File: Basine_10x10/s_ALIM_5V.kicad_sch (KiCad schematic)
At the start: 25 parts, among them U17 TPS5430DDA

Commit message: Basine_10x10
ajout symbole ultrogothe
ajout power flag sur 5V
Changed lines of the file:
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@@
 	(wire
 		(pts
-			(xy 102.87 127) (xy 105.41 127)
+			(xy 102.87 127) (xy 116.84 127)
 		)
 		(stroke
@@
 					(unit 1)
 				)
+			)
+		)
+	)
+	(symbol
+		(lib_name "PWR_FLAG_1")
+		(lib_id "power:PWR_FLAG")
+		(at 116.84 127 0)
+		(unit 1)
+		(exclude_from_sim no)
+		(in_bom yes)
+		(on_board yes)
+		(dnp no)
+		(fields_autoplaced yes)
+		(property "Reference" "#FLG01"
+			(at 116.84 125.095 0)
+			(effects
+				(font
+					(size 1.27 1.27)
+				)
+				(hide yes)
+			)
+		)
+		(property "Value" "PWR_FLAG"
+			(at 116.84 121.92 0)
+			(effects
+				(font
+					(size 1.27 1.27)
+				)
+			)
+		)
+		(property "Footprint" ""
+			(at 116.84 127 0)
+			(effects
+				(font
+					(size 1.27 1.27)
+				)
+				(hide yes)
+			)
+		)
+		(property "Datasheet" "~"
+			(at 116.84 127 0)
+			(effects
+				(font
+					(size 1.27 1.27)
+				)
+				(hide yes)
+			)
+		)
+		(property "Description" "Special symbol for telling ERC where power comes from"
+			(at 116.84 127 0)
+			(effects
+				(font
+					(size 1.27 1.27)
+				)
+				(hide yes)
+			)
+		)
+		(pin "1"
+		)
+		(instances
+			(project "Basine"
+				(path "/e63e39d7-6ac0-4ffd-8aa3-1841a4541b55/c0a1413d-0c72-4618-8b9b-4221cc6761bc"
+					(reference "#FLG01")
+					(unit 1)
+				)

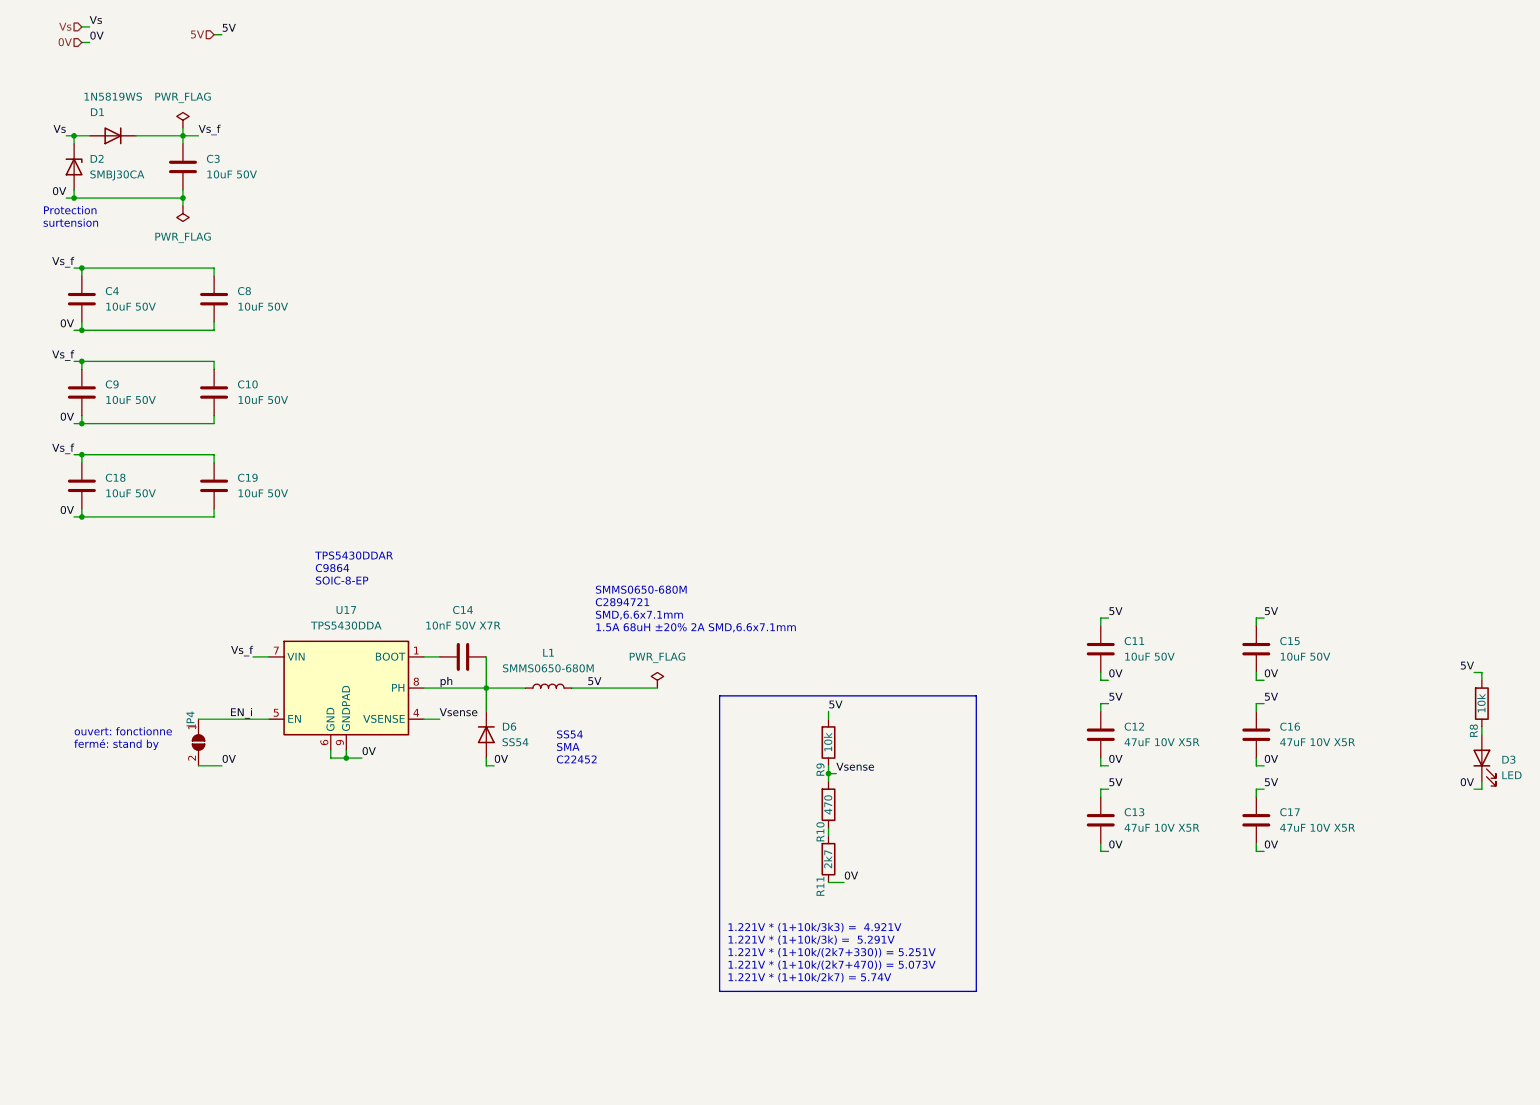
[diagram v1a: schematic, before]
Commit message: 10x10
alim 5V ok
placement et routage ok
reste vias à placer
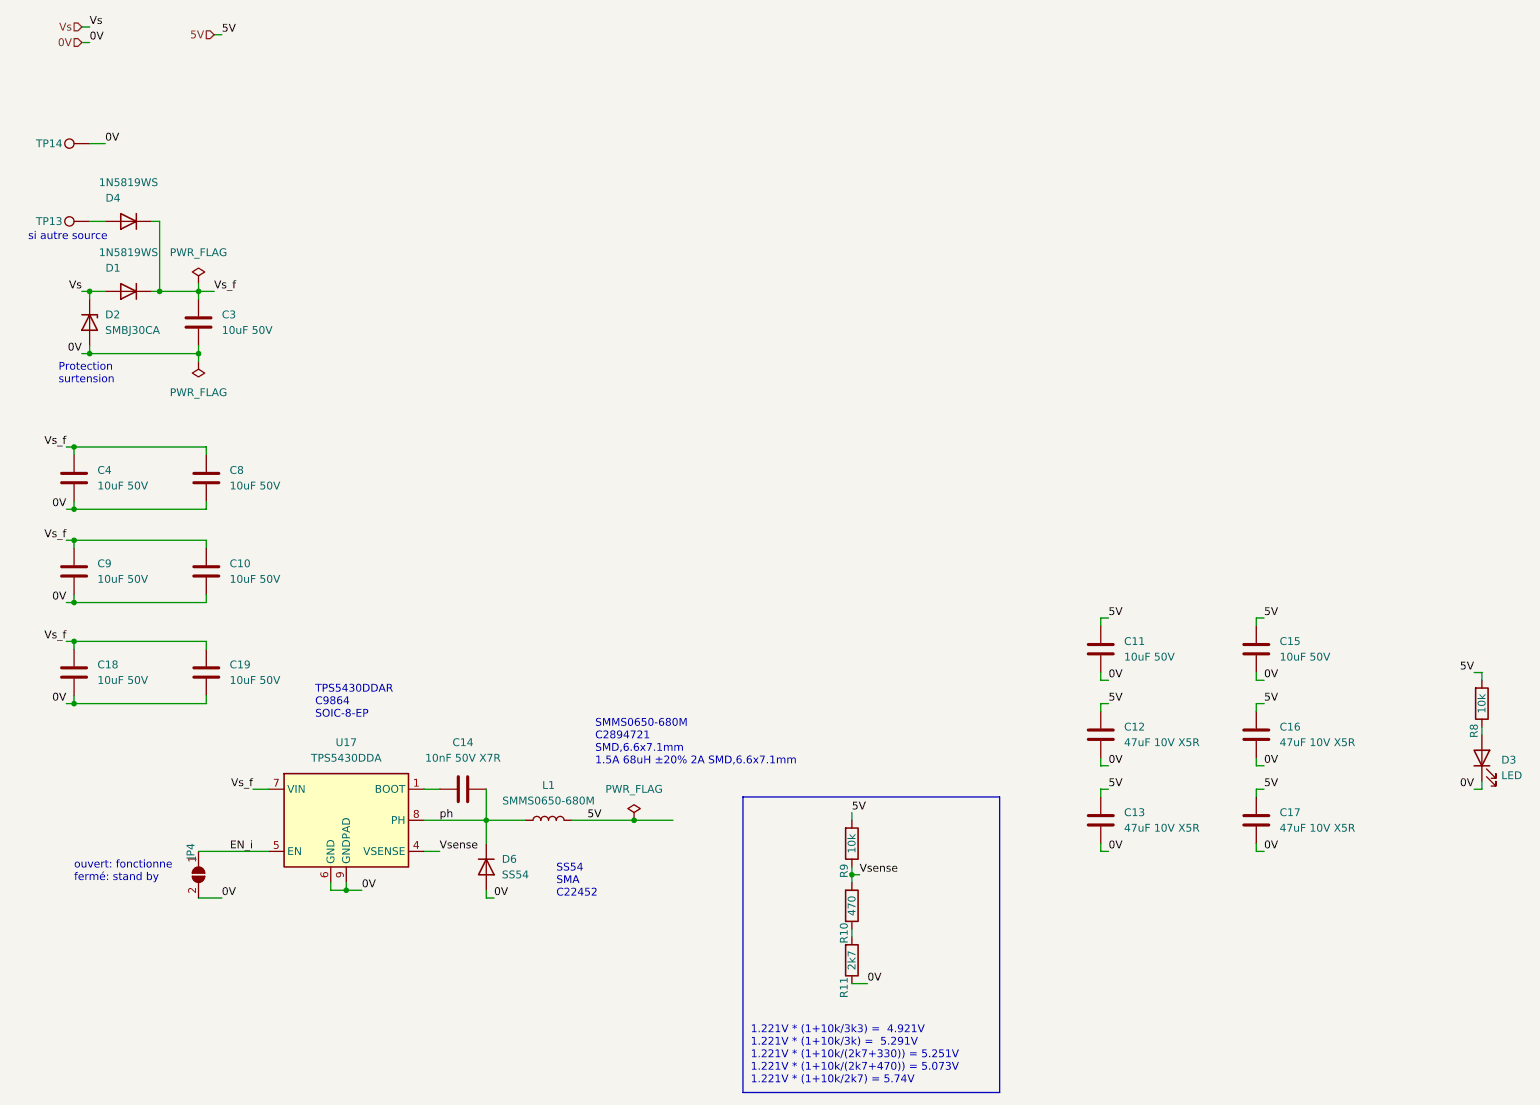
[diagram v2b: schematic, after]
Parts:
- added D4: 1N5819WS, Diode_SMD:D_SOD-323, symbol Device:D
- added TP13, TP14: TestPoint, Chimere_comps:Pastille, symbol Connector:TestPoint
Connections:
- net 0V: now also TP14.1
- net Vs_f: now also D4.1 (K)
- new net: D4.2 (A), TP13.1
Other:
- note added: "si autre source"
- moved on the sheet: C10, C14, C18, C19, C3, C4, C8, C9, D1, D2, D6, JP4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

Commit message: 10x10
tentative de fabrication
pénurie spring clamp à gérer
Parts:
- JP4, TP13, TP14: now left out of the parts list
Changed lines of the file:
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@@
 		(unit 1)
 		(exclude_from_sim no)
-		(in_bom yes)
+		(in_bom no)
 		(on_board yes)
 		(dnp no)
@@
 		(unit 1)
 		(exclude_from_sim no)
-		(in_bom yes)
+		(in_bom no)
 		(on_board yes)
 		(dnp no)
@@
 		(unit 1)
 		(exclude_from_sim no)
-		(in_bom yes)
-		(on_board yes)
-		(dnp no)
+		(in_bom no)
+		(on_board yes)
+		(dnp no)

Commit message: passage au pas de 2,54mm pour toutes les allumettes
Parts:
- removed D4: 1N5819WS, Diode_SMD:D_SOD-323, symbol Device:D
- removed TP13, TP14: TestPoint, Chimere_comps:Pastille, symbol Connector:TestPoint
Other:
- note removed: "si autre source"
